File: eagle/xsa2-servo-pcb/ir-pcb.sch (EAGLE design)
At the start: 39 parts, among them IC1 ATMEGA328P-AU, IC2 PL-IRM0101, IC3 PL-IRM0101, IC4 PL-IRM0101, IC5 PL-IRM0101, IC6 PL-IRM0101, IC7 PL-IRM0101, Q1 IRLML6402, Q2 IRFML8244, Q3 IRFML8244, Q4 IRFML8244, Q5 8MHz, Q6 IRFML8244

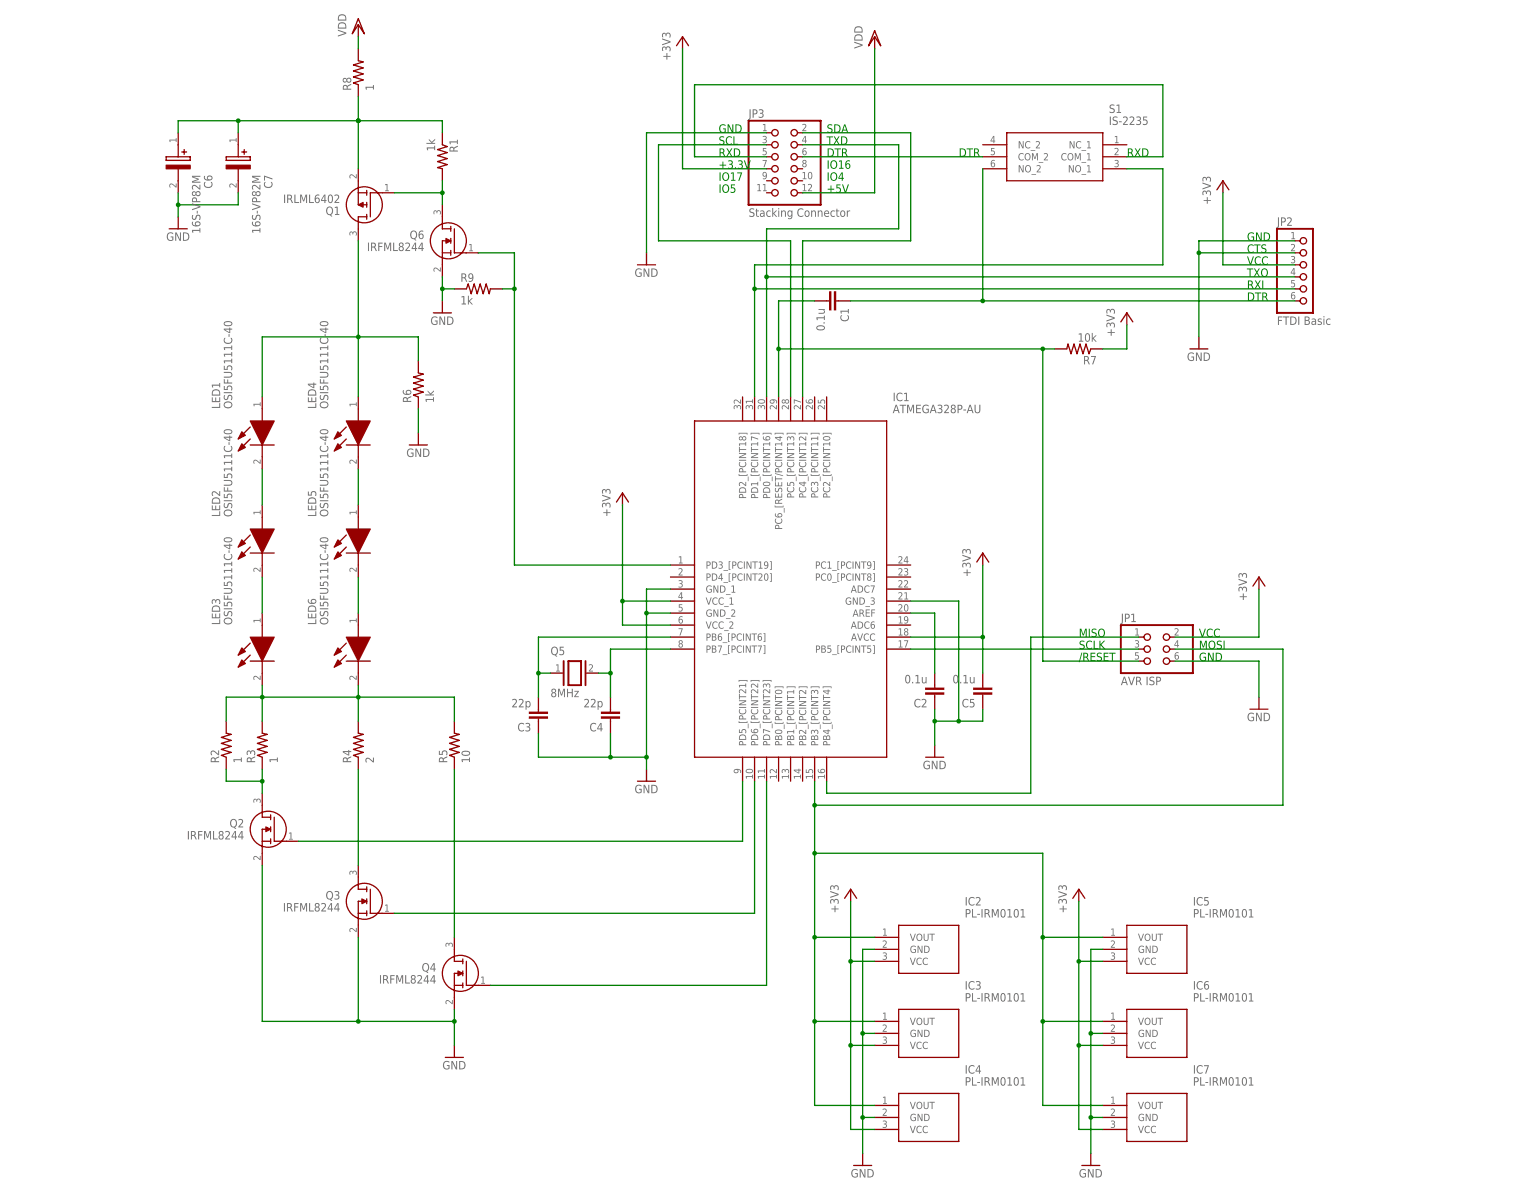
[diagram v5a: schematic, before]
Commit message: [eagle] 連結コネクタのピン数を増加
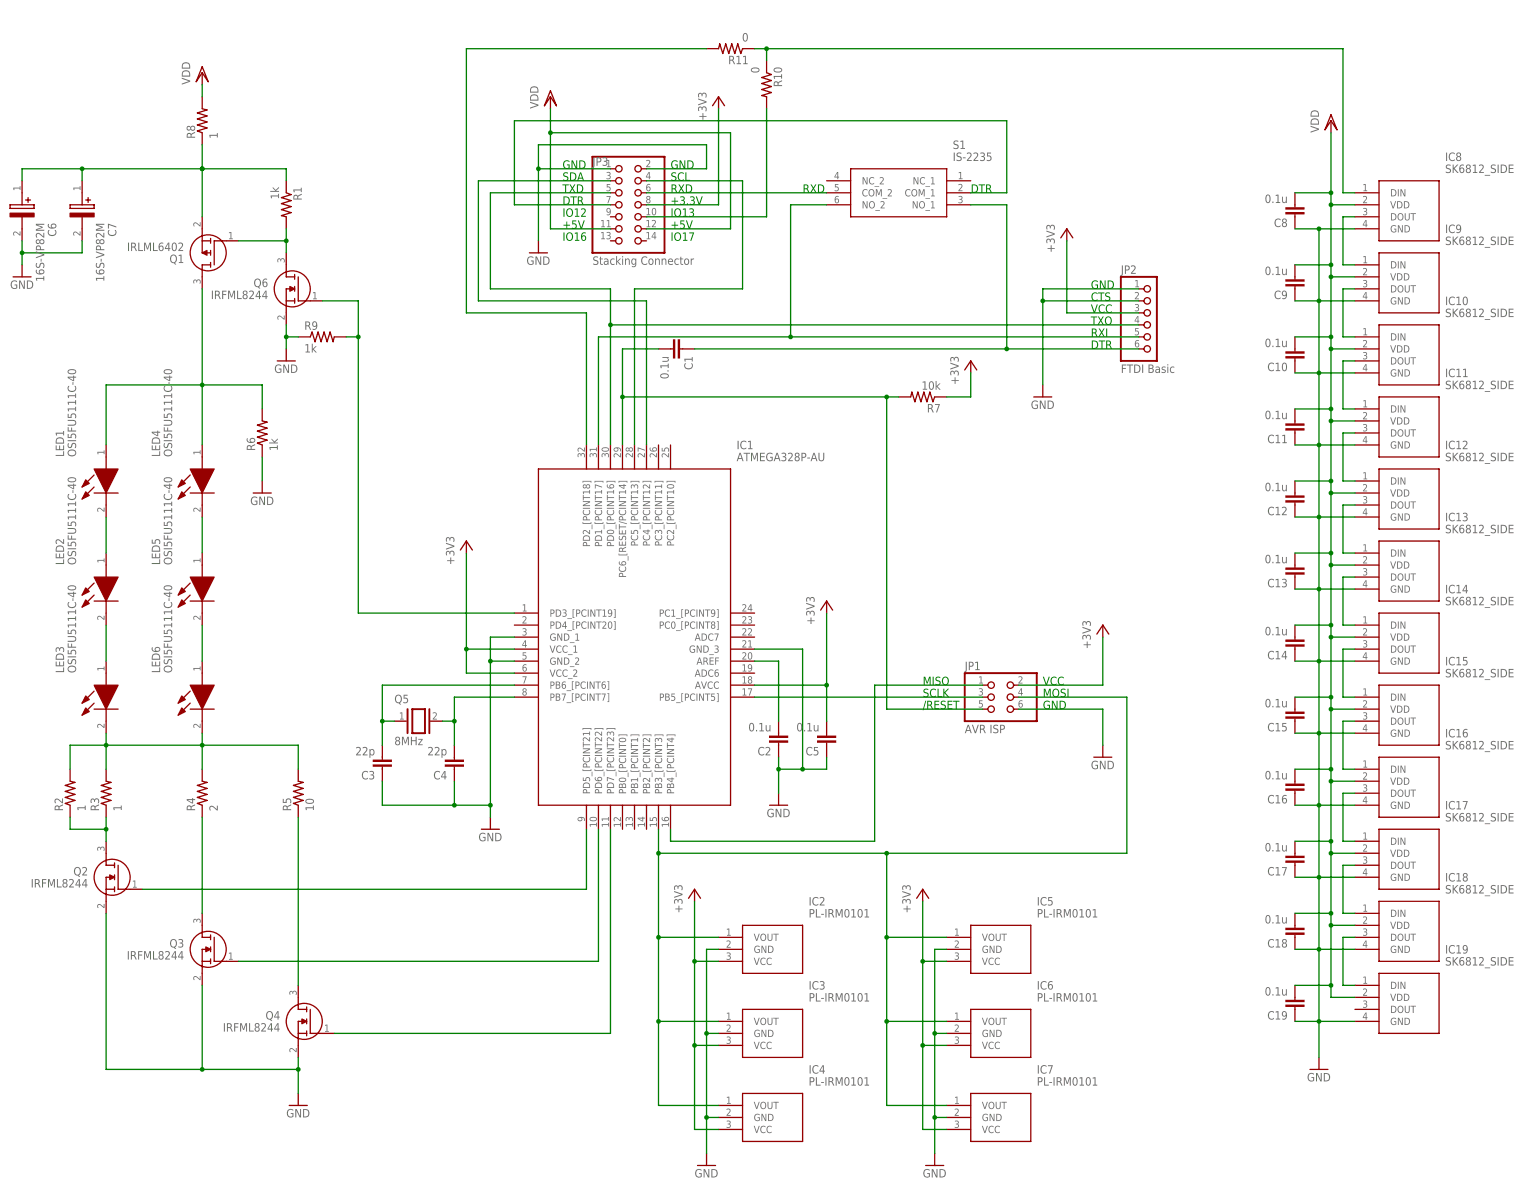
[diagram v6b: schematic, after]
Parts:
- added C10, C11, C12, C13, C14, C15, C16, C17, C18, C19, C8, C9: 0.1u, rcl:C-EUC0603
- added IC10, IC11, IC12, IC13, IC14, IC15, IC16, IC17, IC18, IC19, IC8, IC9: SK6812_SIDE, SamacSys_Parts:SK6812_SIDE
- added R10, R11: 0, rcl:R-US_R0603
- JP2: device pinhead:PINHD-1X6/90 -> pinhead:PINHD-1X6
- JP3: device pinhead:PINHD-2X6 -> pinhead:PINHD-2X7
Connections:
- new net N$30: IC1.PC4_[PCINT12], JP3.3
- new net N$31: IC10.DIN, IC9.DOUT
- new net N$32: IC10.DOUT, IC11.DIN
- new net N$33: IC11.DOUT, IC12.DIN
- new net N$34: IC12.DOUT, IC13.DIN
- new net N$35: IC13.DOUT, IC14.DIN
- new net N$36: IC14.DOUT, IC15.DIN
- new net N$37: IC15.DOUT, IC16.DIN
- new net N$38: IC16.DOUT, IC17.DIN
- new net N$39: IC17.DOUT, IC18.DIN
- new net N$40: IC18.DOUT, IC19.DIN
- new net N$42: JP3.10, R10.2
- new net N$43: IC1.PD2_[PCINT18], R11.2
- new net N$44: IC8.DIN, R10.1, R11.1
- net +3V3: now also JP3.8; no longer JP3.7
- net GND: now also C10.1, C11.1, C12.1, C13.1, C14.1, C15.1, C16.1, C17.1, C18.1, C19.1, C8.1, C9.1, IC10.GND, IC11.GND, IC12.GND, IC13.GND, IC14.GND, IC15.GND, IC16.GND, IC17.GND, IC18.GND, IC19.GND, IC8.GND, IC9.GND, JP3.2
- net N$14: now also JP3.7, S1.COM_1; no longer IC1.PC4_[PCINT12], JP3.2
- net N$21: now also JP3.4; no longer JP3.3
- net N$23: now also JP3.5; no longer JP3.4
- net N$24: now also IC8.DOUT, IC9.DIN; no longer IC1.PD1_[PCINT17], JP2.5, S1.NO_1
- net N$28: now also S1.NO_1; no longer S1.NO_2
- net N$29: now also IC1.PD1_[PCINT17], JP2.5, S1.NO_2; no longer JP3.5, S1.COM_1
- net VDD: now also C10.2, C11.2, C12.2, C13.2, C14.2, C15.2, C16.2, C17.2, C18.2, C19.2, C8.2, C9.2, IC10.VDD, IC11.VDD, IC12.VDD, IC13.VDD, IC14.VDD, IC15.VDD, IC16.VDD, IC17.VDD, IC18.VDD, IC19.VDD, IC8.VDD, IC9.VDD, JP3.11
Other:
- note added: "IO12"
- note added: "IO13"
- note removed: "IO4"
- note removed: "IO5"
- moved on the sheet: C1, C2, C3, C4, C5, C6, C7, IC1, IC2, IC3, IC4, IC5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

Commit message: [eagle] IR基板のパターン設計
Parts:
- removed C6, C7: 16S-VP82M, SamacSys_Parts:16S-VP82M
- removed JP2: FTDI Basic, pinhead:PINHD-1X6
- removed R3, R8: 1, rcl:R-US_R0603
- removed R4: 2, rcl:R-US_R0603
- removed R5: 10, rcl:R-US_R0603
- added C20: 25PFV100M6.3X8, SamacSys_Parts:25PFV100M6.3X8
- added R12: 1, rcl:R-US_R2512W
- added R14: 2, rcl:R-US_R2512W
- added R15: 10, rcl:R-US_R2512W
- R2: value 1 -> 39; device rcl:R-US_R0603 -> rcl:R-US_R2512W
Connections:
- net +3V3: no longer JP2.3
- net GND: now also C20.-; no longer C6.-, C7.-, JP2.1, JP2.2
- net N$12: now also R14.2, R15.2; no longer R3.2, R4.2, R5.2
- net N$15: now also R14.1; no longer R2.1, R3.1
- net N$16: now also R15.1; no longer R4.1
- net N$17: now also R2.1; no longer R5.1
- net N$23: no longer JP2.4
- net N$27: now also C20.+, R12.1; no longer C6.+, C7.+, R8.1
- net N$28: no longer JP2.6
- net N$29: no longer JP2.5
- net VDD: now also R12.2; no longer R8.2
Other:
- note removed: "CTS"
- note removed: "RXI"
- note removed: "TXO"
- moved on the sheet: R2

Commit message: [eagle] サーボ基板完成
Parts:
- removed JP1: AVR ISP, pinhead:PINHD-2X3
- added J1: BM06B-SRSS-TBT_LF__SN_, SamacSys_Parts:BM06B-SRSS-TBT_LF__SN_
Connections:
- net +3V3: now also J1.2; no longer JP1.2
- net GND: now also J1.6; no longer JP1.6
- net N$1: now also J1.1; no longer JP1.1
- net N$25: now also J1.5; no longer JP1.5
- net N$41: now also J1.4; no longer JP1.4
- net N$5: now also J1.3; no longer JP1.3
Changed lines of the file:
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@@
 <part name="LED5" library="SamacSys_Parts" library_urn="urn:adsk.eagle:library:36791783" deviceset="OSI5FU5111C-40" device="" package3d_urn="urn:adsk.eagle:package:36791786/1"/>
 <part name="LED6" library="SamacSys_Parts" library_urn="urn:adsk.eagle:library:36791783" deviceset="OSI5FU5111C-40" device="" package3d_urn="urn:adsk.eagle:package:36791786/1"/>
-<part name="JP1" library="pinhead" library_urn="urn:adsk.eagle:library:325" deviceset="PINHD-2X3" device="" package3d_urn="urn:adsk.eagle:package:22462/2" value="AVR ISP"/>
 <part name="JP3" library="pinhead" library_urn="urn:adsk.eagle:library:325" deviceset="PINHD-2X7" device="" package3d_urn="urn:adsk.eagle:package:22478/2" value="Stacking Connector"/>
 <part name="+3V1" library="supply1" library_urn="urn:adsk.eagle:library:371" deviceset="+3V3" device=""/>
@@
 <part name="R15" library="rcl" library_urn="urn:adsk.eagle:library:334" deviceset="R-US_" device="R2512W" package3d_urn="urn:adsk.eagle:package:23565/2" value="10"/>
 <part name="R2" library="rcl" library_urn="urn:adsk.eagle:library:334" deviceset="R-US_" device="R2512W" package3d_urn="urn:adsk.eagle:package:23565/2" value="39"/>
+<part name="J1" library="SamacSys_Parts" deviceset="BM06B-SRSS-TBT_LF__SN_" device=""/>
 </parts>
 <sheets>
@@
 <text x="0" y="83.82" size="1.778" layer="91">RXD</text>
 <text x="35.56" y="83.82" size="1.778" layer="91">DTR</text>
-<text x="25.4" y="-20.32" size="1.778" layer="91">MISO</text>
-<text x="50.8" y="-20.32" size="1.778" layer="91">VCC</text>
-<text x="25.4" y="-22.86" size="1.778" layer="91">SCLK</text>
-<text x="50.8" y="-22.86" size="1.778" layer="91">MOSI</text>
-<text x="25.4" y="-25.4" size="1.778" layer="91">/RESET</text>
-<text x="50.8" y="-25.4" size="1.778" layer="91">GND</text>
+<text x="25.4" y="5.08" size="1.778" layer="91">MISO</text>
+<text x="25.4" y="2.54" size="1.778" layer="91">VCC</text>
+<text x="25.4" y="0" size="1.778" layer="91">SCLK</text>
+<text x="25.4" y="-2.54" size="1.778" layer="91">MOSI</text>
+<text x="25.4" y="-5.08" size="1.778" layer="91">/RESET</text>
+<text x="27.94" y="-7.62" size="1.778" layer="91">GND</text>
 <text x="-27.94" y="88.9" size="1.778" layer="91">GND</text>
 <text x="-50.8" y="76.2" size="1.778" layer="91">+5V</text>
@@
 <attribute name="VALUE" x="-133.35" y="-17.78" size="1.778" layer="96" rot="R90"/>
 </instance>
-<instance part="JP1" gate="A" x="40.64" y="-22.86" smashed="yes">
-<attribute name="NAME" x="34.29" y="-17.145" size="1.778" layer="95"/>
-<attribute name="VALUE" x="34.29" y="-30.48" size="1.778" layer="96"/>
-</instance>
 <instance part="JP3" gate="A" x="-38.1" y="81.28" smashed="yes">
 <attribute name="NAME" x="-44.45" y="89.535" size="1.778" layer="95"/>
 <attribute name="VALUE" x="-44.45" y="68.58" size="1.778" layer="96"/>
 </instance>
-<instance part="+3V1" gate="G$1" x="63.5" y="-7.62" smashed="yes">
-<attribute name="VALUE" x="60.96" y="-12.7" size="1.778" layer="96" rot="R90"/>
-</instance>
-<instance part="GND1" gate="1" x="63.5" y="-35.56" smashed="yes">
-<attribute name="VALUE" x="60.96" y="-38.1" size="1.778" layer="96"/>
+<instance part="+3V1" gate="G$1" x="22.86" y="15.24" smashed="yes">
+<attribute name="VALUE" x="20.32" y="10.16" size="1.778" layer="96" rot="R90"/>
+</instance>
+<instance part="GND1" gate="1" x="27.94" y="-30.48" smashed="yes">
+<attribute name="VALUE" x="25.4" y="-33.02" size="1.778" layer="96"/>
 </instance>
 <instance part="+3V3" gate="G$1" x="25.4" y="-63.5" smashed="yes">
@@
 <attribute name="NAME" x="-108.1786" y="-46.99" size="1.778" layer="95" rot="R90"/>
 <attribute name="VALUE" x="-103.378" y="-46.99" size="1.778" layer="96" rot="R90"/>
+</instance>
+<instance part="J1" gate="G$1" x="35.56" y="5.08" smashed="yes">
+<attribute name="NAME" x="54.61" y="12.7" size="1.778" layer="95" align="center-left"/>
+<attribute name="VALUE" x="54.61" y="10.16" size="1.778" layer="96" align="center-left"/>
 </instance>
 </instances>
@@
 <segment>
 <pinref part="IC1" gate="G$1" pin="PB5_[PCINT5]"/>
-<wire x1="-10.16" y1="-22.86" x2="38.1" y2="-22.86" width="0.1524" layer="91"/>
-<pinref part="JP1" gate="A" pin="3"/>
+<wire x1="-10.16" y1="-22.86" x2="20.32" y2="-22.86" width="0.1524" layer="91"/>
+<wire x1="20.32" y1="-22.86" x2="20.32" y2="0" width="0.1524" layer="91"/>
+<wire x1="20.32" y1="0" x2="35.56" y2="0" width="0.1524" layer="91"/>
+<pinref part="J1" gate="G$1" pin="3"/>
 </segment>
 </net>
@@
 <segment>
 <pinref part="IC1" gate="G$1" pin="PB4_[PCINT4]"/>
-<pinref part="JP1" gate="A" pin="1"/>
 <wire x1="-27.94" y1="-50.8" x2="-27.94" y2="-53.34" width="0.1524" layer="91"/>
-<wire x1="-27.94" y1="-53.34" x2="15.24" y2="-53.34" width="0.1524" layer="91"/>
-<wire x1="15.24" y1="-53.34" x2="15.24" y2="-20.32" width="0.1524" layer="91"/>
-<wire x1="15.24" y1="-20.32" x2="38.1" y2="-20.32" width="0.1524" layer="91"/>
+<wire x1="-27.94" y1="-53.34" x2="17.78" y2="-53.34" width="0.1524" layer="91"/>
+<wire x1="17.78" y1="-53.34" x2="17.78" y2="5.08" width="0.1524" layer="91"/>
+<wire x1="17.78" y1="5.08" x2="35.56" y2="5.08" width="0.1524" layer="91"/>
+<pinref part="J1" gate="G$1" pin="1"/>
 </segment>
 </net>
@@
 <segment>
 <pinref part="+3V1" gate="G$1" pin="+3V3"/>
-<pinref part="JP1" gate="A" pin="2"/>
-<wire x1="63.5" y1="-10.16" x2="63.5" y2="-20.32" width="0.1524" layer="91"/>
-<wire x1="63.5" y1="-20.32" x2="45.72" y2="-20.32" width="0.1524" layer="91"/>
+<wire x1="22.86" y1="12.7" x2="22.86" y2="2.54" width="0.1524" layer="91"/>
+<wire x1="22.86" y1="2.54" x2="35.56" y2="2.54" width="0.1524" layer="91"/>
+<pinref part="J1" gate="G$1" pin="2"/>
 </segment>
 <segment>
@@
 <net name="GND" class="0">
 <segment>
-<pinref part="JP1" gate="A" pin="6"/>
-<wire x1="45.72" y1="-25.4" x2="63.5" y2="-25.4" width="0.1524" layer="91"/>
+<wire x1="35.56" y1="-7.62" x2="27.94" y2="-7.62" width="0.1524" layer="91"/>
 <pinref part="GND1" gate="1" pin="GND"/>
-<wire x1="63.5" y1="-25.4" x2="63.5" y2="-33.02" width="0.1524" layer="91"/>
+<wire x1="27.94" y1="-7.62" x2="27.94" y2="-27.94" width="0.1524" layer="91"/>
+<pinref part="J1" gate="G$1" pin="6"/>
 </segment>
 <segment>
@@
 <net name="N$25" class="0">
 <segment>
-<pinref part="JP1" gate="A" pin="5"/>
-<wire x1="38.1" y1="-25.4" x2="17.78" y2="-25.4" width="0.1524" layer="91"/>
+<wire x1="35.56" y1="-5.08" x2="15.24" y2="-5.08" width="0.1524" layer="91"/>
 <pinref part="IC1" gate="G$1" pin="PC6_[RESET/PCINT14]"/>
 <wire x1="-38.1" y1="50.8" x2="-38.1" y2="40.64" width="0.1524" layer="91"/>
@@
 <pinref part="C1" gate="G$1" pin="2"/>
 <wire x1="-30.48" y1="50.8" x2="-38.1" y2="50.8" width="0.1524" layer="91"/>
-<wire x1="17.78" y1="-25.4" x2="17.78" y2="40.64" width="0.1524" layer="91"/>
-<wire x1="17.78" y1="40.64" x2="-38.1" y2="40.64" width="0.1524" layer="91"/>
+<wire x1="15.24" y1="-5.08" x2="15.24" y2="40.64" width="0.1524" layer="91"/>
+<wire x1="15.24" y1="40.64" x2="-38.1" y2="40.64" width="0.1524" layer="91"/>
 <junction x="-38.1" y="40.64"/>
 <pinref part="R7" gate="G$1" pin="2"/>
-<wire x1="17.78" y1="40.64" x2="20.32" y2="40.64" width="0.1524" layer="91"/>
-<junction x="17.78" y="40.64"/>
+<wire x1="15.24" y1="40.64" x2="20.32" y2="40.64" width="0.1524" layer="91"/>
+<junction x="15.24" y="40.64"/>
+<pinref part="J1" gate="G$1" pin="5"/>
 </segment>
 </net>
@@
 <wire x1="-30.48" y1="-50.8" x2="-30.48" y2="-55.88" width="0.1524" layer="91"/>
 <wire x1="-30.48" y1="-55.88" x2="17.78" y2="-55.88" width="0.1524" layer="91"/>
-<wire x1="17.78" y1="-55.88" x2="68.58" y2="-55.88" width="0.1524" layer="91"/>
-<wire x1="68.58" y1="-55.88" x2="68.58" y2="-22.86" width="0.1524" layer="91"/>
-<pinref part="JP1" gate="A" pin="4"/>
-<wire x1="68.58" y1="-22.86" x2="45.72" y2="-22.86" width="0.1524" layer="91"/>
+<wire x1="17.78" y1="-55.88" x2="22.86" y2="-55.88" width="0.1524" layer="91"/>
+<wire x1="22.86" y1="-55.88" x2="22.86" y2="-2.54" width="0.1524" layer="91"/>
+<wire x1="22.86" y1="-2.54" x2="35.56" y2="-2.54" width="0.1524" layer="91"/>
 <junction x="-30.48" y="-55.88"/>
 <junction x="17.78" y="-55.88"/>
-</segment>
-</net>
+<pinref part="J1" gate="G$1" pin="4"/>
+</segment>
+</net>
